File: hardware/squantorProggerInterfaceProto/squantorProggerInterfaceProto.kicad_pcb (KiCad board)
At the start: 2 copper layers, 15.9 x 20.9 mm, 24 parts, among them J1 JTAG_interface_proto_input, J2 JTAG_interface_proto_output, U1 74X1T45, U2 74X1T45, U3 74X1T45, U4 74X1T45, U5 74X1G125

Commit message: bottom silk placed
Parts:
- N1: footprint Symbols:OSHW-Symbol_6.7x6mm_SilkScreen -> Symbol:OSHW-Logo_5.7x6mm_SilkScreen
- N2: value 20190703 -> 20190704
- moved N1 7.08 mm to (153.1, 85.4)

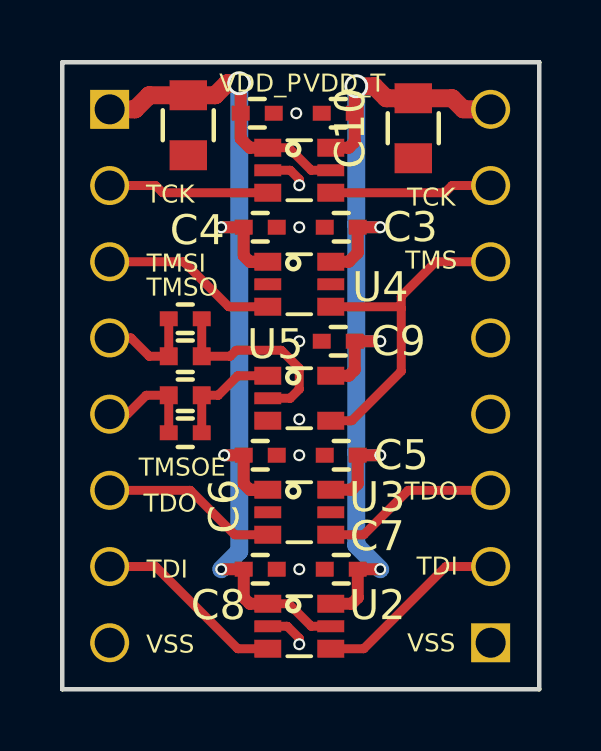
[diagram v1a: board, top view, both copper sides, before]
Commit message: changed OSH logo, front silk mistake fixed
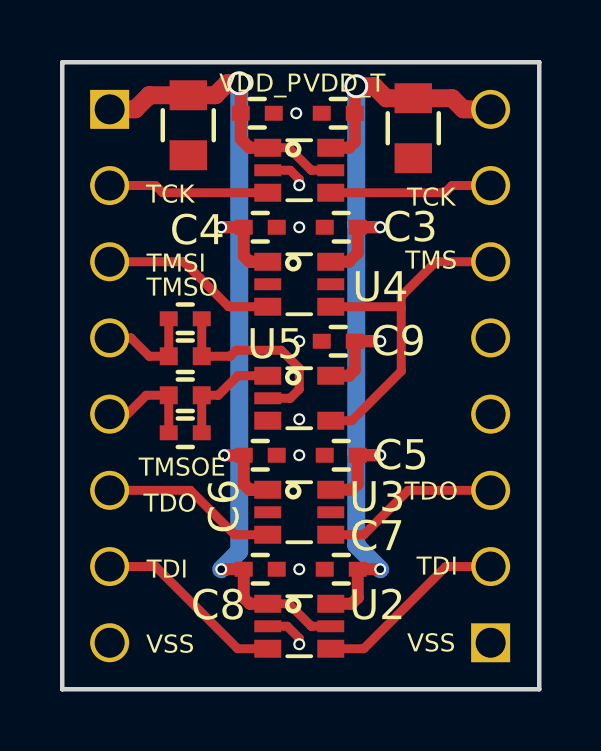
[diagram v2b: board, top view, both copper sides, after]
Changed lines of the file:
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@@
   (page A4)
   (layers
-    (0 F.Cu signal hide)
+    (0 F.Cu signal)
     (31 B.Cu signal)
     (32 B.Adhes user)
@@
     (35 F.Paste user)
     (36 B.SilkS user)
-    (37 F.SilkS user hide)
+    (37 F.SilkS user)
     (38 B.Mask user)
     (39 F.Mask user)
@@
   )
   (setup
-    (last_trace_width 0.6)
+    (last_trace_width 0.1524)
     (user_trace_width 0.1524)
     (user_trace_width 0.2)
@@
     (solder_mask_min_width 0.1)
     (aux_axis_origin 0 0)
-    (visible_elements FFFF7F7F)
+    (visible_elements FFFFFF7F)
     (pcbplotparams
       (layerselection 0x010fc_ffffffff)
@@
     (add_net "Net-(C12-Pad1)")
     (add_net "Net-(C13-Pad1)")
-    (add_net "Net-(J2-Pad4)")
-    (add_net "Net-(J2-Pad5)")
   )
   (module Symbol:OSHW-Logo_5.7x6mm_SilkScreen (layer B.Cu)
@@
     (tags "capacitor 0805")
     (attr smd)
-    (fp_text reference C10 (at 0 -2.1 90) (layer F.SilkS)
-      (effects (font (size 1 1) (thickness 0.15)))
-    )
+    (fp_text reference C10 (at 0 -2.1 90) (layer F.SilkS) hide
+      (effects (font (size 1 1) (thickness 0.15)))
+    )

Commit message: final checks, in production
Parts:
- N2: value 20190704 -> 20190705
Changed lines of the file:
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@@
     (add_net "Net-(C12-Pad1)")
     (add_net "Net-(C13-Pad1)")
+    (add_net "Net-(J2-Pad4)")
+    (add_net "Net-(J2-Pad5)")
   )
   (module Symbol:OSHW-Logo_5.7x6mm_SilkScreen (layer B.Cu)
@@
       (effects (font (size 1 1) (thickness 0.15)) (justify mirror))
     )
-    (fp_text value 20190704 (at -0.4 0.1) (layer B.SilkS)
+    (fp_text value 20190705 (at -0.4 0.1) (layer B.SilkS)
       (effects (font (size 1 1) (thickness 0.15)) (justify mirror))
     )
